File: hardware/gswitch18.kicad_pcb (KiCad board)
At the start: 2 copper layers, 48 x 32 mm, 26 parts, among them P1 JST GHS 1.25, P2 JST GHS 1.25, P3 JST GHS 1.25, P4 USB_B_Mini, P5 ISP, U1 ATMEGA88P, X1 12MHz

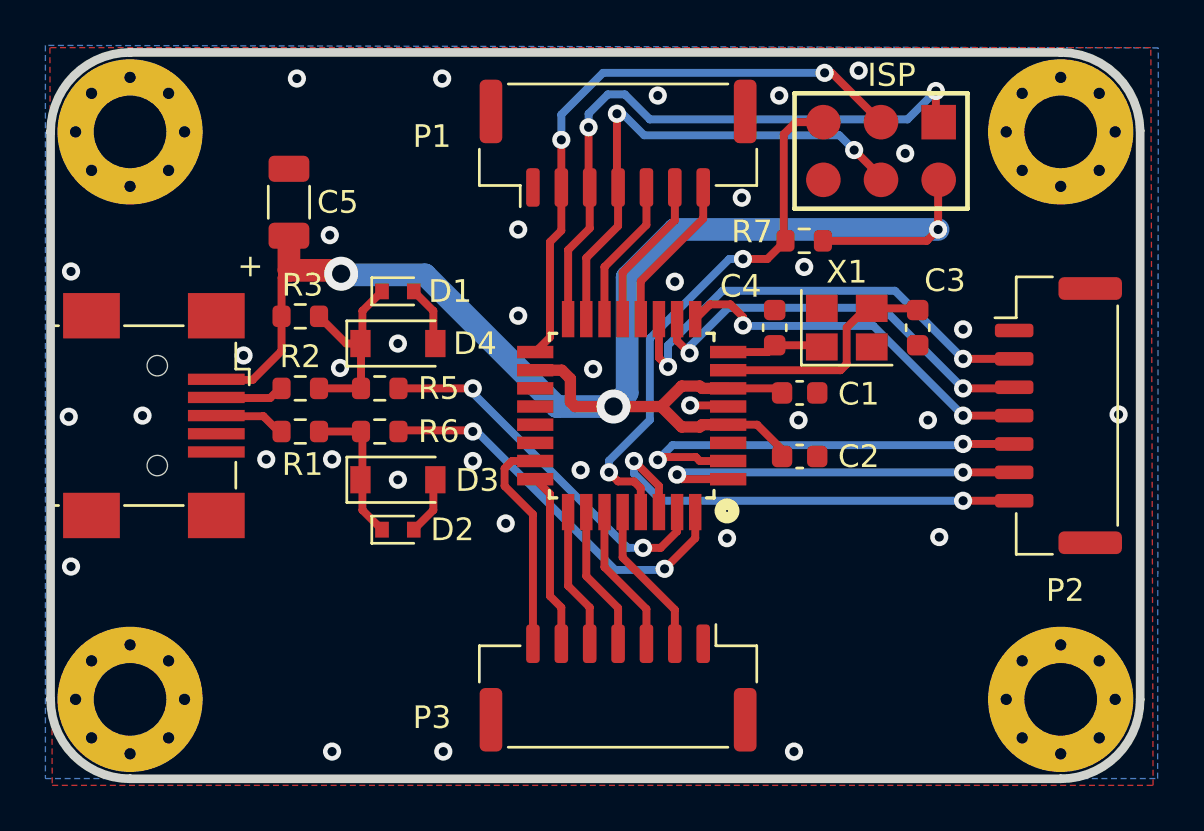
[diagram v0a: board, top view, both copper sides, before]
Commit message: SMD: All JLCPCB part codes loaded. Other fixes.
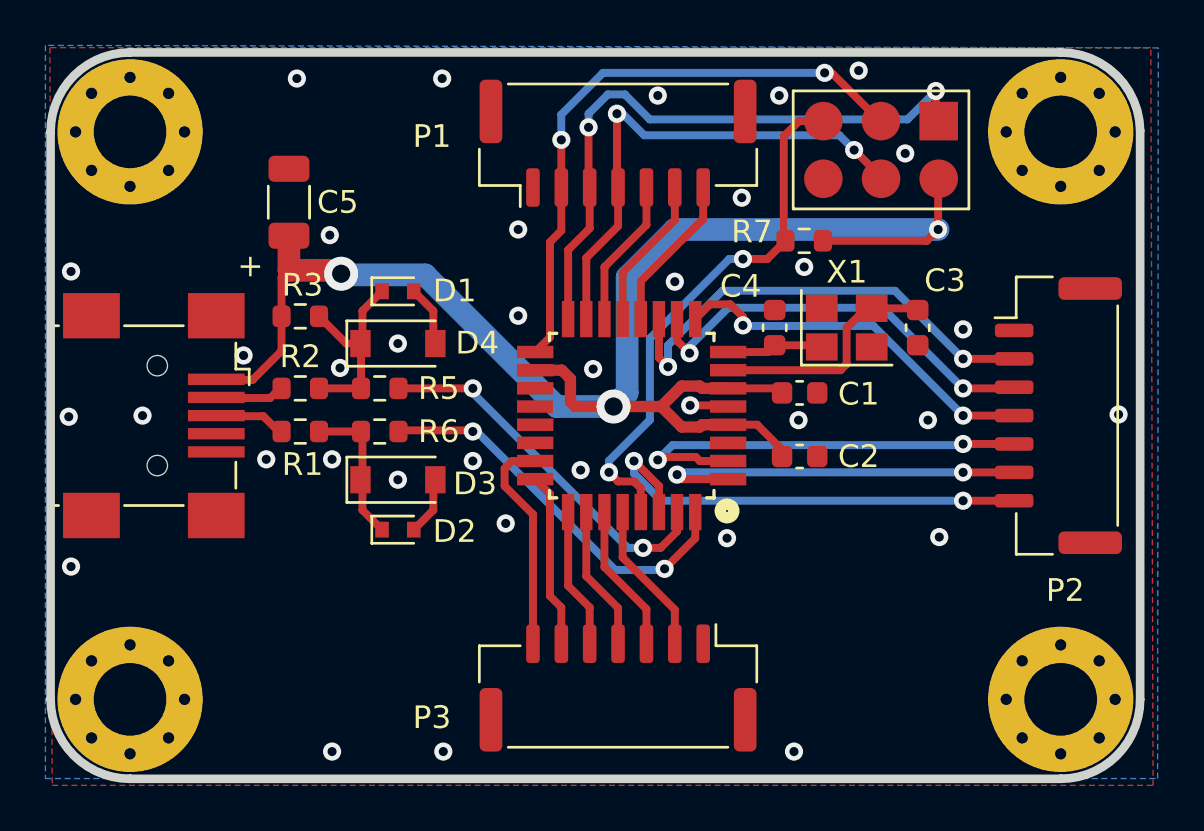
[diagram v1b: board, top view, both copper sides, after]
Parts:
- C5: value 10u tant. -> 10uF 16V Tantalum
- D1, D2: value Sctky -> 200mA
- D3, D4: value 3V6 -> 3V6 500mW
- MH1, MH2, MH3, MH4: value via pad -> 3.2mm
- P5: footprint pin_array_3x2 -> Connector_PinHeader_2.54mm:PinHeader_2x03_P2.54mm_Vertical
- moved P5 2.86 mm to (115.1, 53.8), turned to -90 degrees
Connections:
- D1 pad 1: GND -> Net-(R3-Pad2)
- D1 pad 2: Net-(D1-Pad2) -> GND
- D2 pad 1: GND -> Net-(R1-Pad1)
- D2 pad 2: Net-(D2-Pad2) -> GND
- D3 pad 1: GND -> Net-(R1-Pad1)
- D3 pad 2: Net-(D2-Pad2) -> GND
- D4 pad 1: GND -> Net-(R3-Pad2)
- D4 pad 2: Net-(D1-Pad2) -> GND
- R1 pad 1: Net-(D2-Pad2) -> Net-(R1-Pad1)
- R2 pad 1: Net-(D1-Pad2) -> Net-(R3-Pad2)
- R3 pad 2: Net-(D1-Pad2) -> Net-(R3-Pad2)
- R5 pad 2: Net-(D1-Pad2) -> Net-(R3-Pad2)
- R6 pad 2: Net-(D2-Pad2) -> Net-(R1-Pad1)
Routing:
- net Net-(R3-Pad2): track 0.00 -> 8.83 mm
- net Net-(D1-Pad2): track 8.83 -> 0.00 mm
- net Net-(R1-Pad1): track 0.00 -> 6.56 mm
- net Net-(D2-Pad2): track 6.56 -> 0.00 mm
